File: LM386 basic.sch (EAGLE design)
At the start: 11 parts, among them IC1 LM386N-3

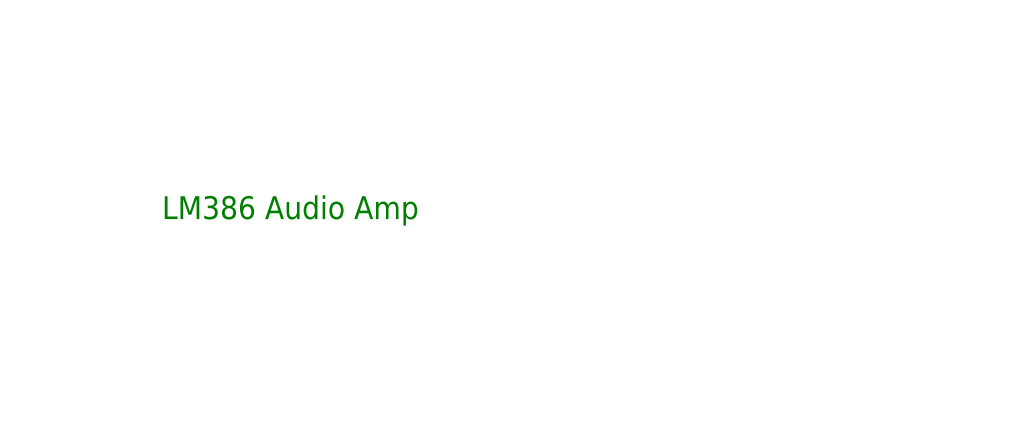
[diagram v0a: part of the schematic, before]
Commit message: added info to title block
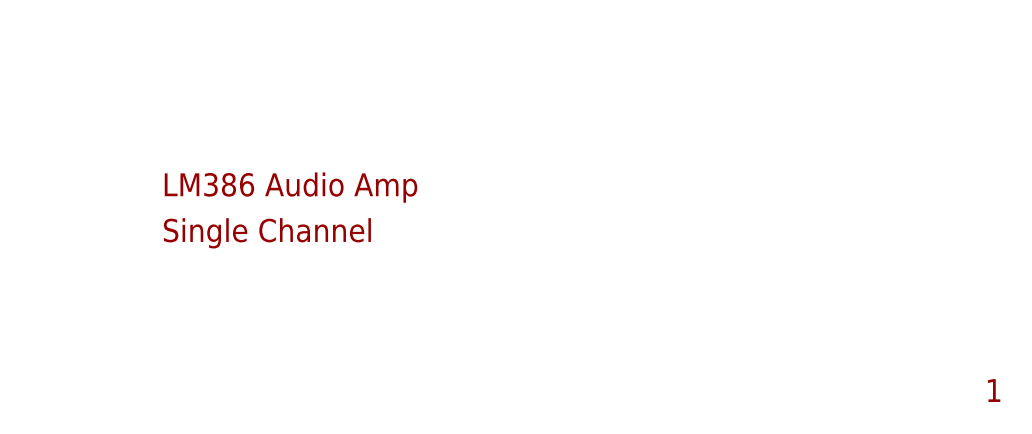
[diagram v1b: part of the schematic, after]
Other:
- note added: "1"
- note added: "Single Channel"
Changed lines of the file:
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@@
 <sheet>
 <plain>
-<text x="175.26" y="27.94" size="2.54" layer="91">LM386 Audio Amp</text>
+<text x="175.26" y="30.48" size="2.54" layer="94">LM386 Audio Amp</text>
 <text x="86.36" y="119.38" size="1.778" layer="91">PWR</text>
 <text x="86.36" y="147.32" size="1.778" layer="91">AUDIN</text>
@@
 <text x="193.04" y="121.92" size="1.778" layer="91">+
 -</text>
+<text x="175.26" y="25.4" size="2.54" layer="94">Single Channel</text>
+<text x="266.7" y="7.62" size="2.54" layer="94">1</text>
 </plain>
 <instances>
